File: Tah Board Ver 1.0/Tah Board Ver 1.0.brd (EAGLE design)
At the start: 39 x 55.2 mm, 31 parts, among them J1 AVR_SPI_PRG, U1 ATMEGA32U4, U2 3.3V_REG_LDOSMD

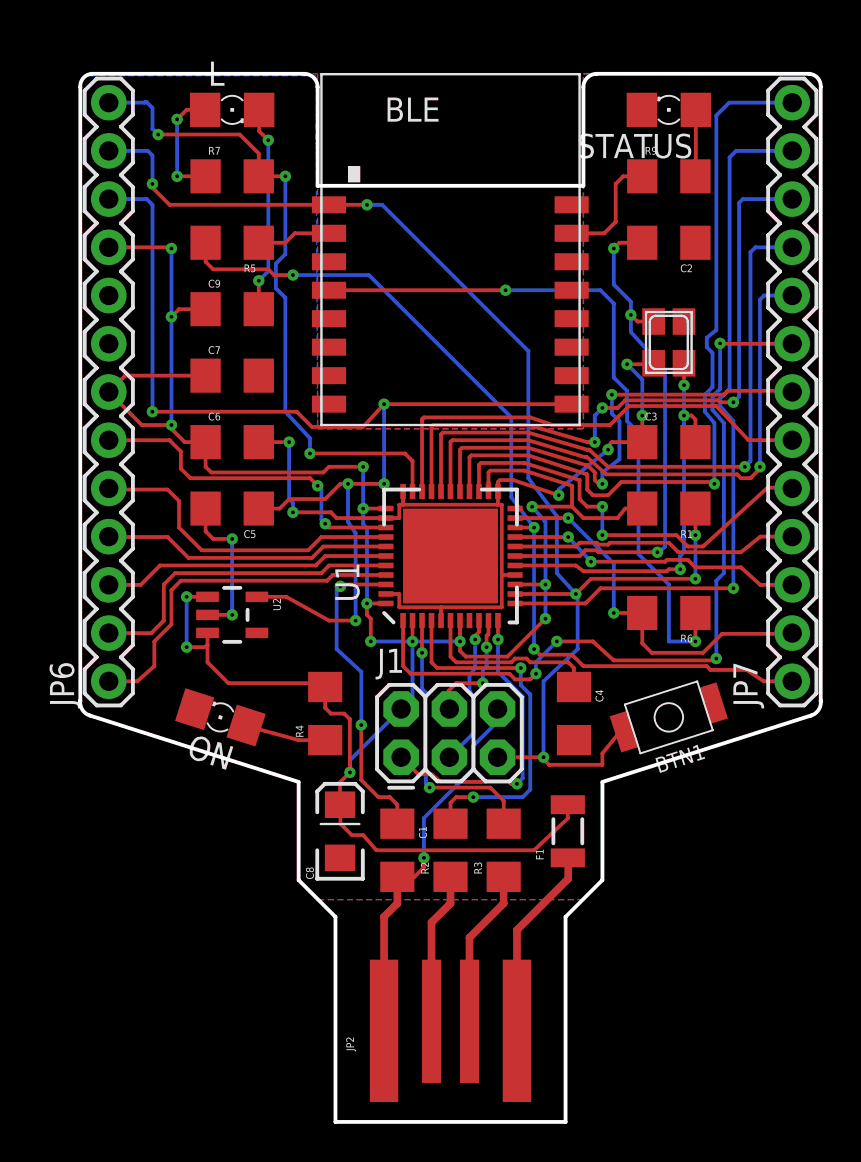
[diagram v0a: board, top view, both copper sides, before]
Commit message: Updated production ready files for Tah and shields
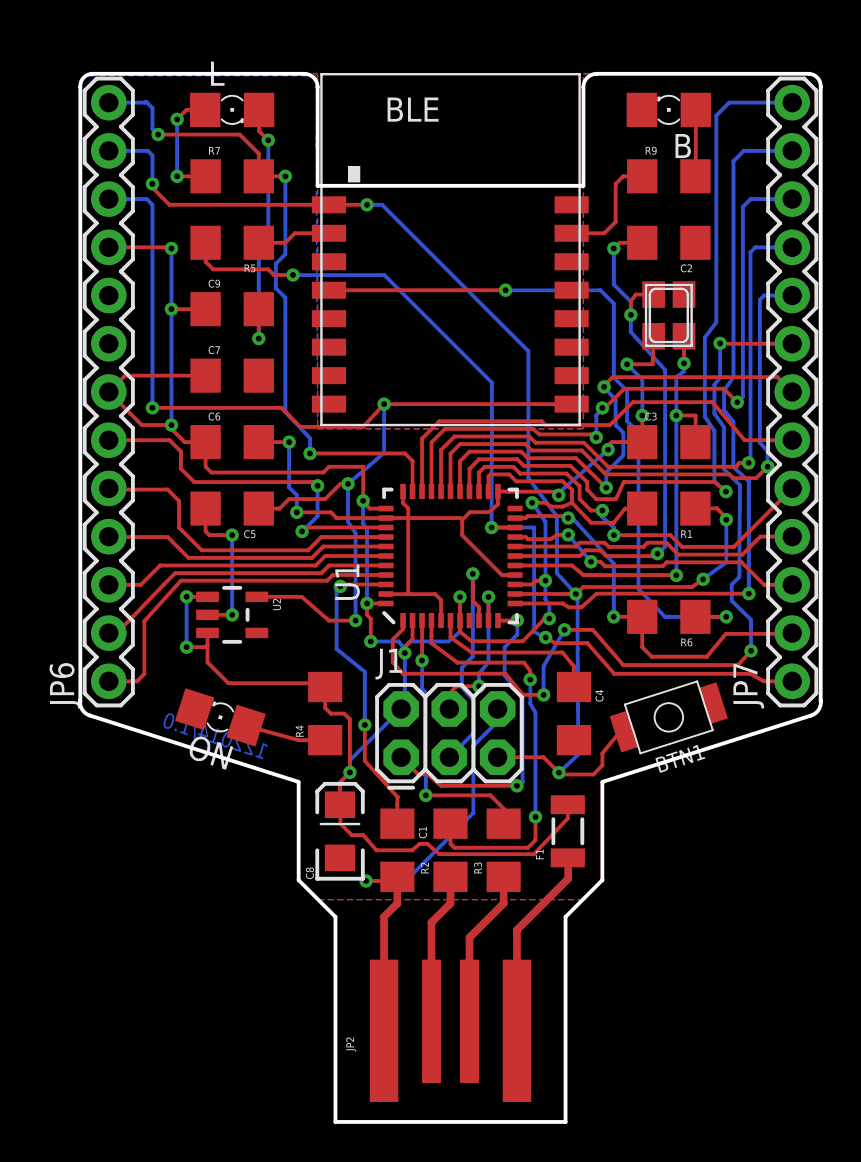
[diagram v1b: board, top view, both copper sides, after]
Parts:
- L: value Yellow -> Green
- ON: value Green -> Red
- U1: device SparkFun-DigitalIC:QFN-44 -> SparkFun-Retired:SPARKFUN-DIGITALIC_QFN-44-NOPAD
- moved Q1 1.42 mm to (31.0, 42.7)
- moved R6 0.20 mm to (31.0, 26.8)
- renumbered STATUS to B
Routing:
- net GND: track 86.6 -> 93.1 mm
- net D7: track 41.8 -> 47.1 mm
- net SCK: track 7.97 -> 13.2 mm
- net RST: track 72.1 -> 75.3 mm
- net N$6: track 19.2 -> 21.8 mm
- net MOSI: track 6.37 -> 8.69 mm
- net N$3: track 21.7 -> 23.9 mm
- net A0: track 18.0 -> 19.8 mm
- net TX: track 48.3 -> 49.9 mm
- net D6: track 25.4 -> 26.8 mm
- net MISO: track 15.9 -> 17.2 mm
- net 5V: track 128.0 -> 129.1 mm, vias 15 -> 14
- net A4: track 17.2 -> 16.1 mm
- net 3.3V: track 60.4 -> 59.4 mm, vias 5 -> 4
- net D11: track 38.4 -> 39.4 mm
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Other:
- board text added: "122014/1.0"
- board text added: "http://tah.io/start"
- board text removed: "tah.io/start"
